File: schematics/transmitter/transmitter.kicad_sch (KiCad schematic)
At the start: 27 parts, among them Q1 2N7000, SW1 SW_Nidec_CAS-120A1, SW2 SW_Push, U1 PIC16F18324-xSL, U2 NRF24L01_Breakout, U3 LM2937xT

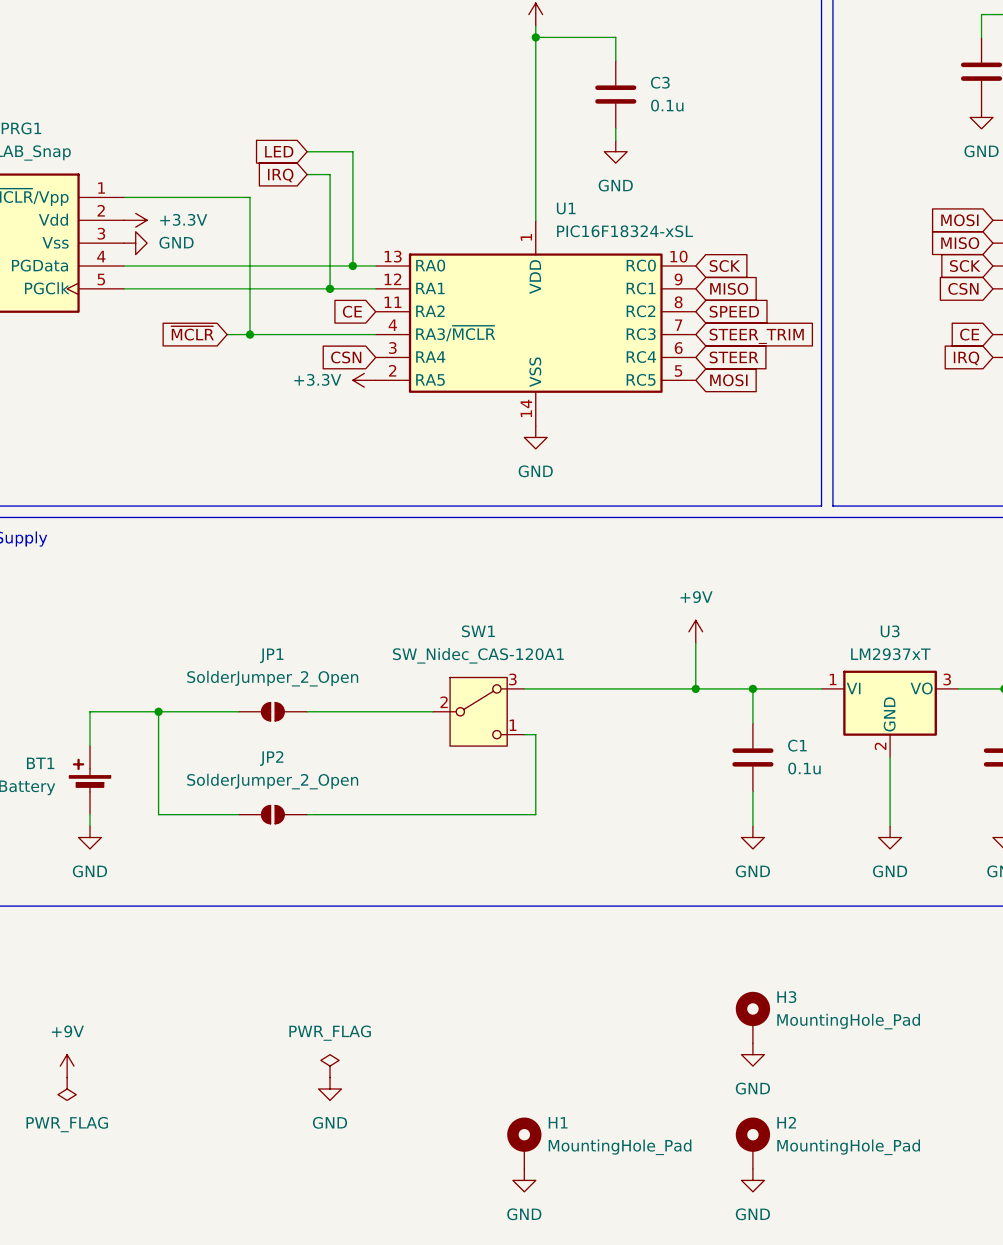
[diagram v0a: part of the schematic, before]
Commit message: Remove unnecessary devices
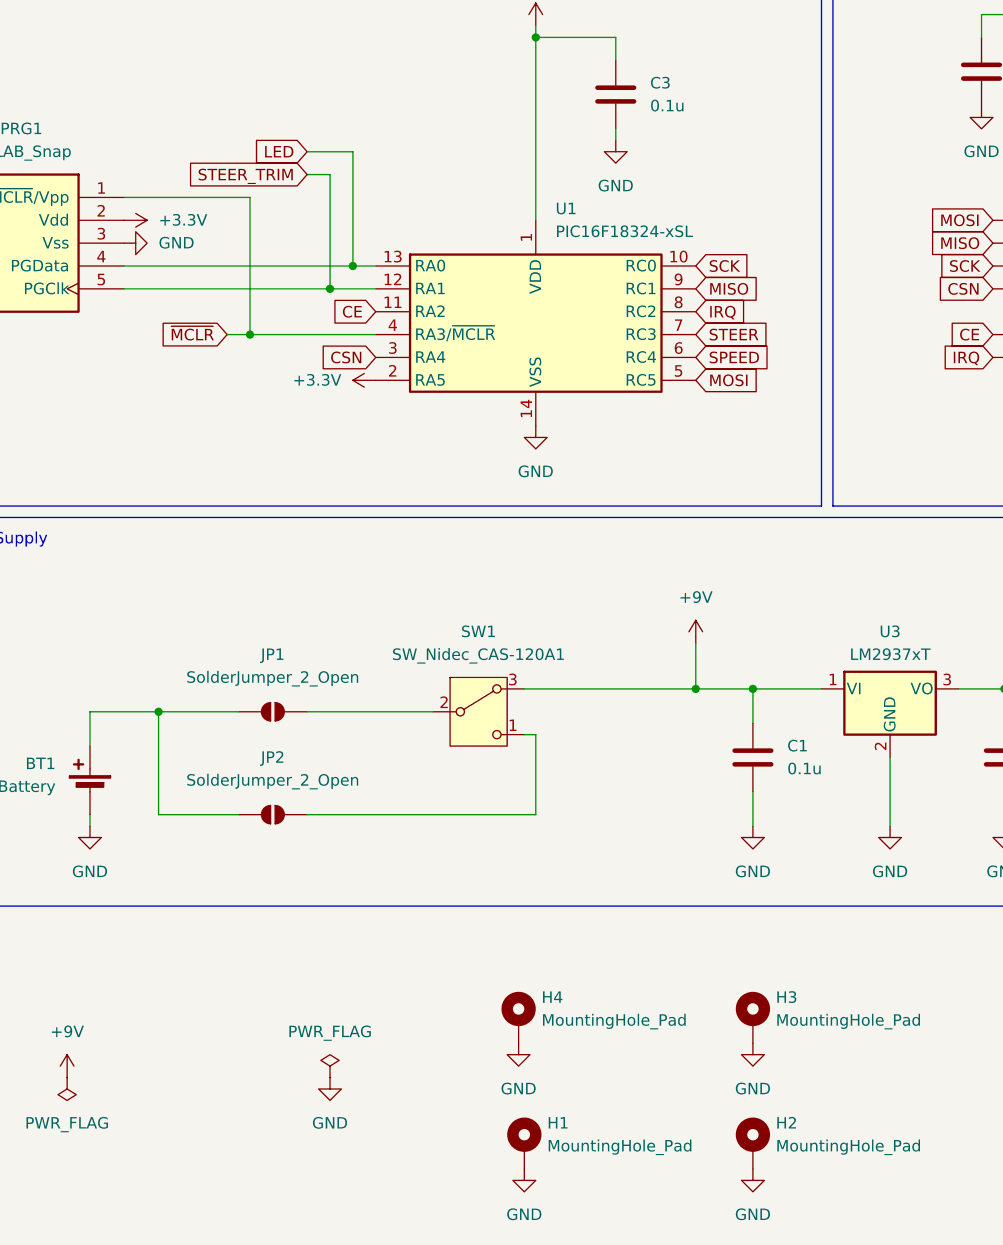
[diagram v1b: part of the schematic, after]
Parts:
- added H4: MountingHole_Pad, MountingHole:MountingHole_2.5mm_Pad_TopBottom, symbol Mechanical:MountingHole_Pad
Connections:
- net GND: now also H4.1
- net IRQ: now also U1.8 (RC2); no longer PRG1.5 (PGClk), U1.12 (RA1)
- net SPEED: now also U1.6 (RC4); no longer U1.8 (RC2)
- net STEER: now also U1.7 (RC3); no longer U1.6 (RC4)
- net STEER_TRIM: now also PRG1.5 (PGClk), U1.12 (RA1); no longer U1.7 (RC3)
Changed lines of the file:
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@@
 	(global_label "IRQ"
 		(shape input)
-		(at 68.58 72.39 180)
+		(at 111.76 87.63 0)
 		(fields_autoplaced yes)
 		(effects
@@
 				(size 1.27 1.27)
 			)
-			(justify right)
+			(justify left)
 		)
 		(property "Intersheetrefs" "${INTERSHEET_REFS}"
-			(at 62.3895 72.39 0)
+			(at 117.9505 87.63 0)
 			(effects
 				(font
 					(size 1.27 1.27)
 				)
-				(justify right)
+				(justify left)
 				(hide yes)
 			)
@@
 	(global_label "STEER_TRIM"
 		(shape input)
-		(at 111.76 90.17 0)
+		(at 68.58 72.39 180)
 		(fields_autoplaced yes)
 		(effects
@@
 				(size 1.27 1.27)
 			)
-			(justify left)
+			(justify right)
 		)
 		(property "Intersheetrefs" "${INTERSHEET_REFS}"
-			(at 125.7517 90.17 0)
+			(at 54.5883 72.39 0)
 			(effects
 				(font
 					(size 1.27 1.27)
 				)
-				(justify left)
+				(justify right)
 				(hide yes)
 			)
@@
 	(global_label "SPEED"
 		(shape input)
-		(at 111.76 87.63 0)
+		(at 111.76 92.71 0)
 		(fields_autoplaced yes)
 		(effects
@@
 		)
 		(property "Intersheetrefs" "${INTERSHEET_REFS}"
-			(at 120.7927 87.63 0)
+			(at 120.7927 92.71 0)
 			(effects
 				(font
@@
 	(global_label "STEER"
 		(shape input)
-		(at 111.76 92.71 0)
+		(at 111.76 90.17 0)
 		(fields_autoplaced yes)
 		(effects
@@
 		)
 		(property "Intersheetrefs" "${INTERSHEET_REFS}"
-			(at 120.4903 92.71 0)
+			(at 120.4903 90.17 0)
 			(effects
 				(font
@@
 		(exclude_from_sim no)
 		(in_bom yes)
-		(on_board yes)
+		(on_board no)
 		(dnp no)
 		(fields_autoplaced yes)
@@
 		(exclude_from_sim no)
 		(in_bom yes)
-		(on_board yes)
+		(on_board no)
 		(dnp no)
 		(fields_autoplaced yes)
@@
 		(exclude_from_sim no)
 		(in_bom yes)
-		(on_board yes)
+		(on_board no)
 		(dnp no)
 		(fields_autoplaced yes)
@@
 		(exclude_from_sim no)
 		(in_bom yes)
-		(on_board yes)
+		(on_board no)
 		(dnp no)
 		(fields_autoplaced yes)
@@
 	(symbol
 		(lib_id "power:GND")
-		(at 210.82 144.78 0)
+		(at 92.075 168.91 0)
 		(unit 1)
 		(exclude_from_sim no)
@@
 		(dnp no)
 		(fields_autoplaced yes)
+		(property "Reference" "#PWR033"
+			(at 92.075 175.26 0)
+			(effects
+				(font
+					(size 1.27 1.27)
+				)
+				(hide yes)
+			)
+		)
+		(property "Value" "GND"
+			(at 92.075 173.99 0)
+			(effects
+				(font
+					(size 1.27 1.27)
+				)
+			)
+		)
+		(property "Footprint" ""
+			(at 92.075 168.91 0)
+			(effects
+				(font
+					(size 1.27 1.27)
+				)
+				(hide yes)
+			)
+		)
+		(property "Datasheet" ""
+			(at 92.075 168.91 0)
+			(effects
+				(font
+					(size 1.27 1.27)
+				)
+				(hide yes)
+			)
+		)
+		(property "Description" "Power symbol creates a global label with name \"GND\" , ground"
+			(at 92.075 168.91 0)
+			(effects
+				(font
+					(size 1.27 1.27)
+				)
+				(hide yes)
+			)
+		)
+		(pin "1"
+		)
+		(instances
+			(project "transmitter"
+				(path "/8cd5d3cf-8985-42c2-bd7d-5d07b5ac3cd8"
+					(reference "#PWR033")
+					(unit 1)
+				)
+			)
+		)
+	)
+	(symbol
+		(lib_id "power:GND")
+		(at 210.82 144.78 0)
+		(unit 1)
+		(exclude_from_sim no)
+		(in_bom yes)
+		(on_board no)
+		(dnp no)
+		(fields_autoplaced yes)
 		(property "Reference" "#PWR011"
 			(at 210.82 151.13 0)
@@
 		(exclude_from_sim no)
 		(in_bom yes)
-		(on_board yes)
+		(on_board no)
 		(dnp no)
 		(fields_autoplaced yes)
@@
 		(exclude_from_sim no)
 		(in_bom yes)
-		(on_board yes)
+		(on_board no)
 		(dnp no)
 		(fields_autoplaced yes)
@@
 		(exclude_from_sim no)
 		(in_bom yes)
-		(on_board yes)
+		(on_board no)
 		(dnp no)
 		(fields_autoplaced yes)
@@
 		(exclude_from_sim no)
 		(in_bom yes)
-		(on_board yes)
+		(on_board no)
 		(dnp no)
 		(fields_autoplaced yes)
@@
 	)
 	(symbol
+		(lib_id "Mechanical:MountingHole_Pad")
+		(at 92.075 166.37 0)
+		(unit 1)
+		(exclude_from_sim yes)
+		(in_bom no)
+		(on_board yes)
+		(dnp no)
+		(fields_autoplaced yes)
+		(property "Reference" "H4"
+			(at 94.615 163.8299 0)
+			(effects
+				(font
+					(size 1.27 1.27)
+				)
+				(justify left)
+			)
+		)
+		(property "Value" "MountingHole_Pad"
+			(at 94.615 166.3699 0)
+			(effects
+				(font
+					(size 1.27 1.27)
+				)
+				(justify left)
+			)
+		)
+		(property "Footprint" "MountingHole:MountingHole_2.5mm_Pad_TopBottom"
+			(at 92.075 166.37 0)
+			(effects
+				(font
+					(size 1.27 1.27)
+				)
+				(hide yes)
+			)
+		)
+		(property "Datasheet" "~"
+			(at 92.075 166.37 0)
+			(effects
+				(font
+					(size 1.27 1.27)
+				)
+				(hide yes)
+			)
+		)
+		(property "Description" "Mounting Hole with connection"
+			(at 92.075 166.37 0)
+			(effects
+				(font
+					(size 1.27 1.27)
+				)
+				(hide yes)
+			)
+		)
+		(property "Mfn" ""
+			(at 92.075 166.37 0)
+			(effects
+				(font
+					(size 1.27 1.27)
+				)
+				(hide yes)
+			)
+		)
+		(property "Mfn PN" ""
+			(at 92.075 166.37 0)
+			(effects
+				(font
+					(size 1.27 1.27)
+				)
+				(hide yes)
+			)
+		)
+		(property "Supplier" ""
+			(at 92.075 166.37 0)
+			(effects
+				(font
+					(size 1.27 1.27)
+				)
+				(hide yes)
+			)
+		)
+		(property "Supplier PN" ""
+			(at 92.075 166.37 0)
+			(effects
+				(font
+					(size 1.27 1.27)
+				)
+				(hide yes)
+			)
+		)
+		(pin "1"
+		)
+		(instances
+			(project "transmitter"
+				(path "/8cd5d3cf-8985-42c2-bd7d-5d07b5ac3cd8"
+					(reference "H4")
+					(unit 1)
+				)
+			)
+		)
+	)
+	(symbol
 		(lib_id "power:GND")
 		(at 44.45 144.78 0)
@@
 		(exclude_from_sim no)
 		(in_bom yes)
-		(on_board yes)
+		(on_board no)
 		(dnp no)
 		(fields_autoplaced yes)

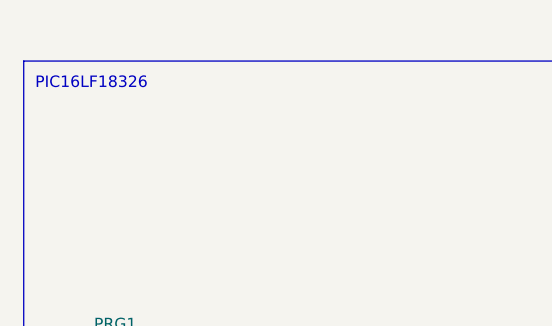
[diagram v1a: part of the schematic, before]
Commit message: Add schematic titles
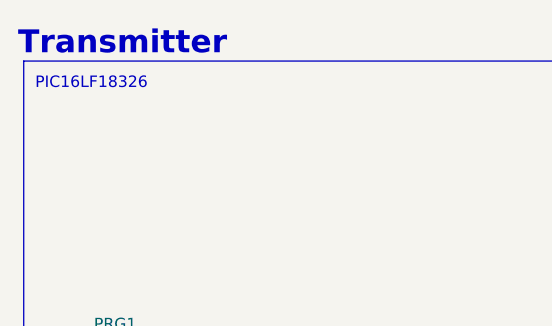
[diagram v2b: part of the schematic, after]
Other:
- note added: "Transmitter"
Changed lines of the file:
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@@
+		)
+	)
+	(text "Transmitter"
+		(exclude_from_sim no)
+		(at 26.035 36.195 0)
+		(effects
+			(font
+				(size 2.54 2.54)
+				(thickness 0.508)
+				(bold yes)
+			)
+			(justify left)
 		)
 	)

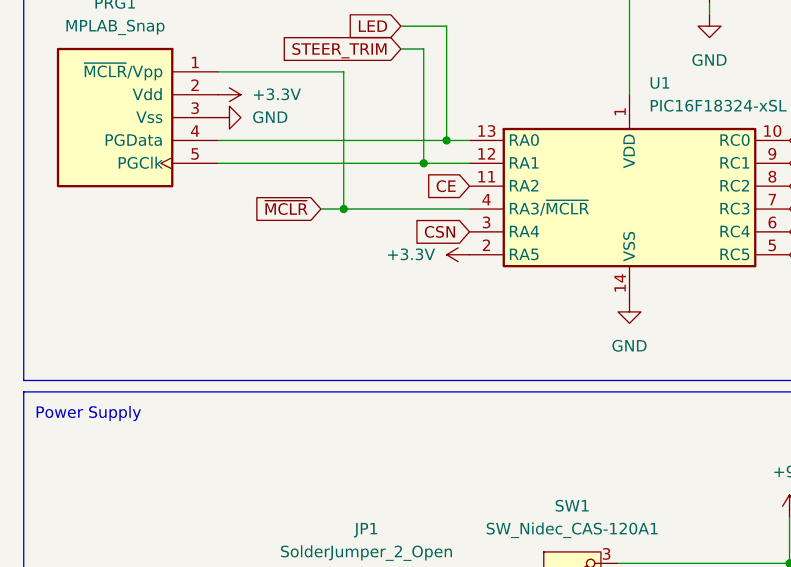
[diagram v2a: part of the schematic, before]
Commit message: Add pull up for TX mcu select
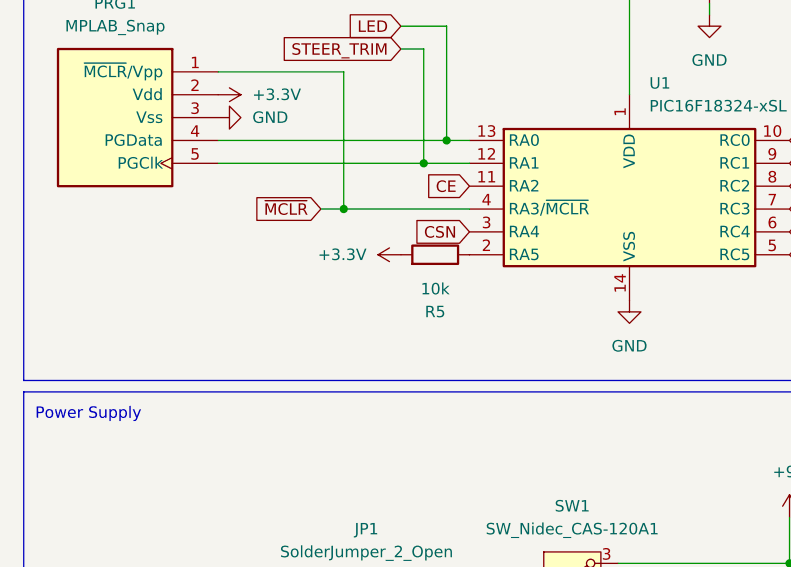
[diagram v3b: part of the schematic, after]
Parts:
- added R5: 10k, Resistor_THT:R_Axial_DIN0204_L3.6mm_D1.6mm_P7.62mm_Horizontal, symbol Device:R
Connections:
- net +3.3V: now also R5.2; no longer U1.2 (RA5)
- new net: R5.1, U1.2 (RA5)
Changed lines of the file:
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@@
 	(symbol
 		(lib_id "power:+3.3V")
-		(at 76.2 95.25 90)
-		(unit 1)
-		(exclude_from_sim no)
-		(in_bom yes)
-		(on_board yes)
-		(dnp no)
-		(fields_autoplaced yes)
+		(at 68.58 95.25 90)
+		(unit 1)
+		(exclude_from_sim no)
+		(in_bom yes)
+		(on_board yes)
+		(dnp no)
 		(property "Reference" "#PWR027"
-			(at 80.01 95.25 0)
+			(at 72.39 95.25 0)
 			(effects
 				(font
@@
 		)
 		(property "Value" "+3.3V"
-			(at 72.39 95.2499 90)
+			(at 64.77 95.2499 90)
 			(effects
 				(font
@@
 		)
 		(property "Footprint" ""
-			(at 76.2 95.25 0)
+			(at 68.58 95.25 0)
 			(effects
 				(font
@@
 		)
 		(property "Datasheet" ""
-			(at 76.2 95.25 0)
+			(at 68.58 95.25 0)
 			(effects
 				(font
@@
 		)
 		(property "Description" "Power symbol creates a global label with name \"+3.3V\""
-			(at 76.2 95.25 0)
+			(at 68.58 95.25 0)
 			(effects
 				(font
@@
 					(unit 1)
 				)
+			)
+		)
+	)
+	(symbol
+		(lib_id "Device:R")
+		(at 72.39 95.25 270)
+		(mirror x)
+		(unit 1)
+		(exclude_from_sim no)
+		(in_bom yes)
+		(on_board yes)
+		(dnp no)
+		(property "Reference" "R5"
+			(at 72.39 101.6 90)
+			(effects
+				(font
+					(size 1.27 1.27)
+				)
+			)
+		)
+		(property "Value" "10k"
+			(at 72.39 99.06 90)
+			(effects
+				(font
+					(size 1.27 1.27)
+				)
+			)
+		)
+		(property "Footprint" "Resistor_THT:R_Axial_DIN0204_L3.6mm_D1.6mm_P7.62mm_Horizontal"
+			(at 72.39 97.028 90)
+			(effects
+				(font
+					(size 1.27 1.27)
+				)
+				(hide yes)
+			)
+		)
+		(property "Datasheet" "~"
+			(at 72.39 95.25 0)
+			(effects
+				(font
+					(size 1.27 1.27)
+				)
+				(hide yes)
+			)
+		)
+		(property "Description" "Resistor"
+			(at 72.39 95.25 0)
+			(effects
+				(font
+					(size 1.27 1.27)
+				)
+				(hide yes)
+			)
+		)
+		(property "Mfn" ""
+			(at 72.39 95.25 0)
+			(effects
+				(font
+					(size 1.27 1.27)
+				)
+				(hide yes)
+			)
+		)
+		(property "Mfn PN" ""
+			(at 72.39 95.25 0)
+			(effects
+				(font
+					(size 1.27 1.27)
+				)
+				(hide yes)
+			)
+		)
+		(property "Supplier" ""
+			(at 72.39 95.25 0)
+			(effects
+				(font
+					(size 1.27 1.27)
+				)
+				(hide yes)
+			)
+		)
+		(property "Supplier PN" ""
+			(at 72.39 95.25 0)
+			(effects
+				(font
+					(size 1.27 1.27)
+				)
+				(hide yes)
+			)
+		)
+		(pin "2"
+		)
+		(pin "1"
+		)
+		(instances
+			(project "transmitter"
+				(path "/8cd5d3cf-8985-42c2-bd7d-5d07b5ac3cd8"
+					(reference "R5")
+					(unit 1)
+				)

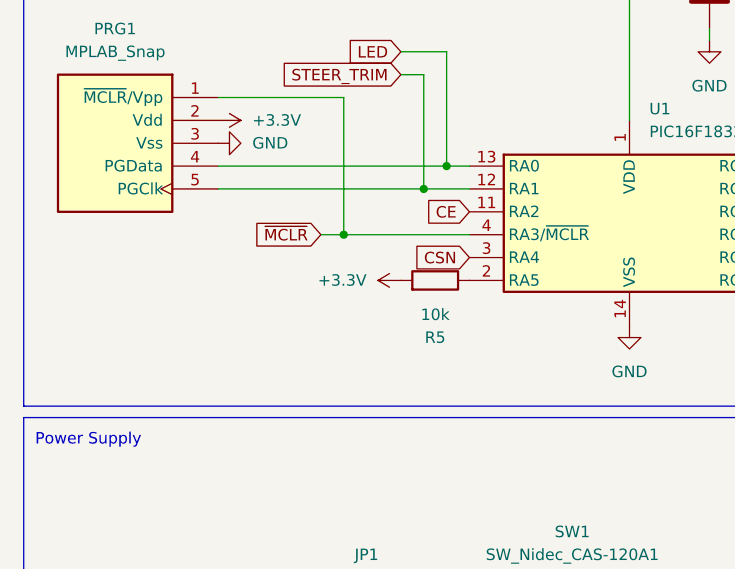
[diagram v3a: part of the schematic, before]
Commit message: Add pull down for lights on transmitter board
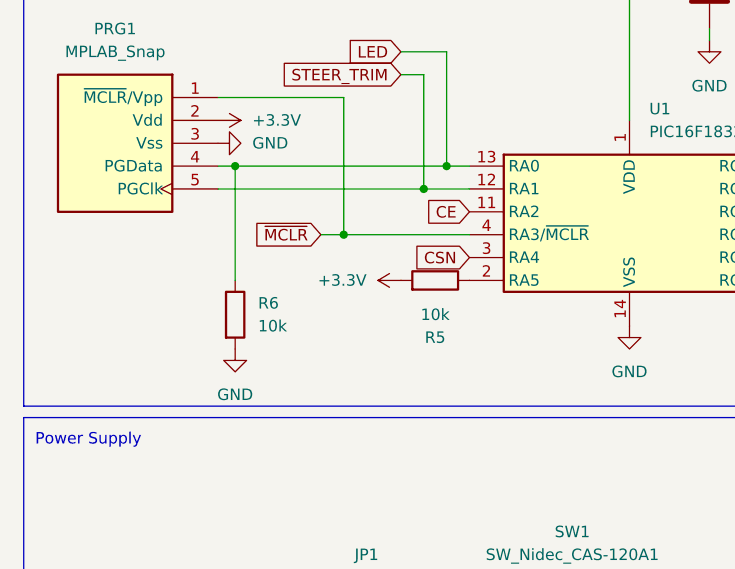
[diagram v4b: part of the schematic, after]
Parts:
- added R6: 10k, Resistor_THT:R_Axial_DIN0204_L3.6mm_D1.6mm_P7.62mm_Horizontal, symbol Device:R
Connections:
- net GND: now also R6.2
- net LED: now also R6.1
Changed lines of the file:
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@@
+	)
+	(junction
+		(at 50.165 82.55)
+		(diameter 0)
+		(color 0 0 0 0)
 	)
 	(junction
@@
 	(wire
 		(pts
-			(xy 48.26 82.55) (xy 73.66 82.55)
+			(xy 48.26 82.55) (xy 50.165 82.55)
 		)
 		(stroke
@@
 	(wire
 		(pts
+			(xy 50.165 82.55) (xy 73.66 82.55)
+		)
+		(stroke
+			(width 0)
+			(type default)
+		)
+	)
+	(wire
+		(pts
 			(xy 44.45 132.08) (xy 52.07 132.08)
 		)
@@
 		(pts
 			(xy 93.98 143.51) (xy 68.58 143.51)
+		)
+		(stroke
+			(width 0)
+			(type default)
+		)
+	)
+	(wire
+		(pts
+			(xy 50.165 82.55) (xy 50.165 95.25)
 		)
 		(stroke
@@
 	(symbol
 		(lib_id "power:GND")
+		(at 50.165 102.87 0)
+		(unit 1)
+		(exclude_from_sim no)
+		(in_bom yes)
+		(on_board yes)
+		(dnp no)
+		(fields_autoplaced yes)
+		(property "Reference" "#PWR034"
+			(at 50.165 109.22 0)
+			(effects
+				(font
+					(size 1.27 1.27)
+				)
+				(hide yes)
+			)
+		)
+		(property "Value" "GND"
+			(at 50.165 107.95 0)
+			(effects
+				(font
+					(size 1.27 1.27)
+				)
+			)
+		)
+		(property "Footprint" ""
+			(at 50.165 102.87 0)
+			(effects
+				(font
+					(size 1.27 1.27)
+				)
+				(hide yes)
+			)
+		)
+		(property "Datasheet" ""
+			(at 50.165 102.87 0)
+			(effects
+				(font
+					(size 1.27 1.27)
+				)
+				(hide yes)
+			)
+		)
+		(property "Description" "Power symbol creates a global label with name \"GND\" , ground"
+			(at 50.165 102.87 0)
+			(effects
+				(font
+					(size 1.27 1.27)
+				)
+				(hide yes)
+			)
+		)
+		(pin "1"
+		)
+		(instances
+			(project "transmitter"
+				(path "/8cd5d3cf-8985-42c2-bd7d-5d07b5ac3cd8"
+					(reference "#PWR034")
+					(unit 1)
+				)
+			)
+		)
+	)
+	(symbol
+		(lib_id "power:GND")
 		(at 133.35 144.78 0)
 		(unit 1)
@@
 					(unit 1)
 				)
+			)
+		)
+	)
+	(symbol
+		(lib_id "Device:R")
+		(at 50.165 99.06 0)
+		(unit 1)
+		(exclude_from_sim no)
+		(in_bom yes)
+		(on_board yes)
+		(dnp no)
+		(fields_autoplaced yes)
+		(property "Reference" "R6"
+			(at 52.705 97.7899 0)
+			(effects
+				(font
+					(size 1.27 1.27)
+				)
+				(justify left)
+			)
+		)
+		(property "Value" "10k"
+			(at 52.705 100.3299 0)
+			(effects
+				(font
+					(size 1.27 1.27)
+				)
+				(justify left)
+			)
+		)
+		(property "Footprint" "Resistor_THT:R_Axial_DIN0204_L3.6mm_D1.6mm_P7.62mm_Horizontal"
+			(at 48.387 99.06 90)
+			(effects
+				(font
+					(size 1.27 1.27)
+				)
+				(hide yes)
+			)
+		)
+		(property "Datasheet" "~"
+			(at 50.165 99.06 0)
+			(effects
+				(font
+					(size 1.27 1.27)
+				)
+				(hide yes)
+			)
+		)
+		(property "Description" "Resistor"
+			(at 50.165 99.06 0)
+			(effects
+				(font
+					(size 1.27 1.27)
+				)
+				(hide yes)
+			)
+		)
+		(property "Mfn" ""
+			(at 50.165 99.06 0)
+			(effects
+				(font
+					(size 1.27 1.27)
+				)
+				(hide yes)
+			)
+		)
+		(property "Mfn PN" ""
+			(at 50.165 99.06 0)
+			(effects
+				(font
+					(size 1.27 1.27)
+				)
+				(hide yes)
+			)
+		)
+		(property "Supplier" ""
+			(at 50.165 99.06 0)
+			(effects
+				(font
+					(size 1.27 1.27)
+				)
+				(hide yes)
+			)
+		)
+		(property "Supplier PN" ""
+			(at 50.165 99.06 0)
+			(effects
+				(font
+					(size 1.27 1.27)
+				)
+				(hide yes)
+			)
+		)
+		(pin "2"
+		)
+		(pin "1"
+		)
+		(instances
+			(project "transmitter"
+				(path "/8cd5d3cf-8985-42c2-bd7d-5d07b5ac3cd8"
+					(reference "R6")
+					(unit 1)
+				)
